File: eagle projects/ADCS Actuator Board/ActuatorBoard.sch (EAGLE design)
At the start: 231 parts, among them J11 TE_1-84953-1, J2 TE_1-84953-1, J4 TE_1-84953-1, J5 TE-1734829-3, U1 SIP2100DY-T1-GE3, U10 LM2917MX/NOPB, U12 TSV991AILT, U13 LM2917MX/NOPB, U14 ADS7841E_2K5, U16 DRV10970_MOTOR_DRIVERDRV10970, U17 LM2917MX/NOPB, U19 TSV991AILT, U2 SIP2100DY-T1-GE3, U20 ADS7841E_2K5, U3 SIP2100DY-T1-GE3, U6 DRV10970_MOTOR_DRIVERDRV10970, U7 DRV10970_MOTOR_DRIVERDRV10970, U8 TSV991AILT, U9 ADS7841E_2K5

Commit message: done
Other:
- note added: "ADCS Electrical"
- note added: "B"
- note added: "J. Smith, T.Christison"
- note added: "Maxon 351098"
- note removed: "A.1"
- note removed: "FIN 0 1 0 1 PWM 0 1 PWM"
- note removed: "OUT1 Hi-Z 1 0 0 1 !PWM !PWM 0"
- note removed: "OUT2 Hi-Z 0 1 0 !PWM 1 0 !PWM"
- note removed: "Operation Mode Stand-by Forward Reverse Brake Forward (PWM mode A) Reverse (PWM mode A) Forward (PWM mode B) Reverse (PWM mode B)"
- note removed: "RIN 0 0 1 1 0 PWM PWM 1"
- note removed: "VREF X VCC VCC X VCC VCC VCC VCC"

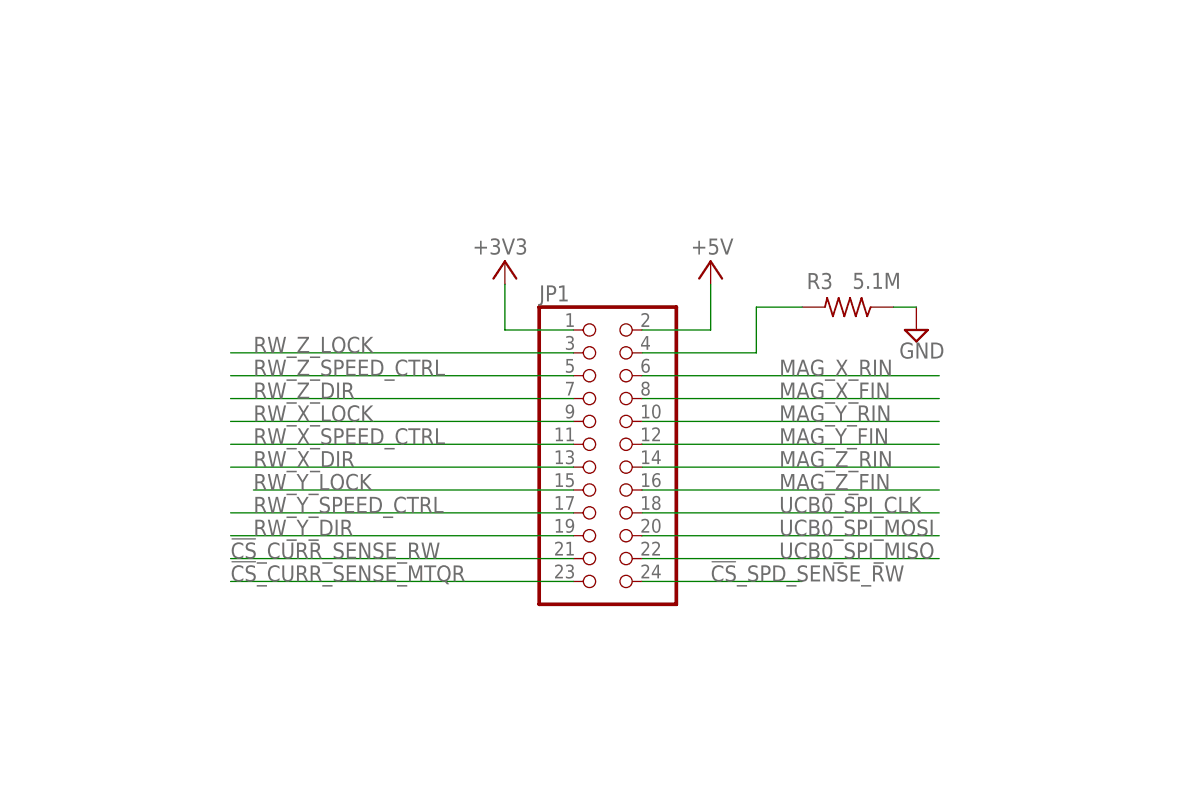
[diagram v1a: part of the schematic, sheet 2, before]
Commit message: Partially Replaced Connectors on Actuator
Will finish soon
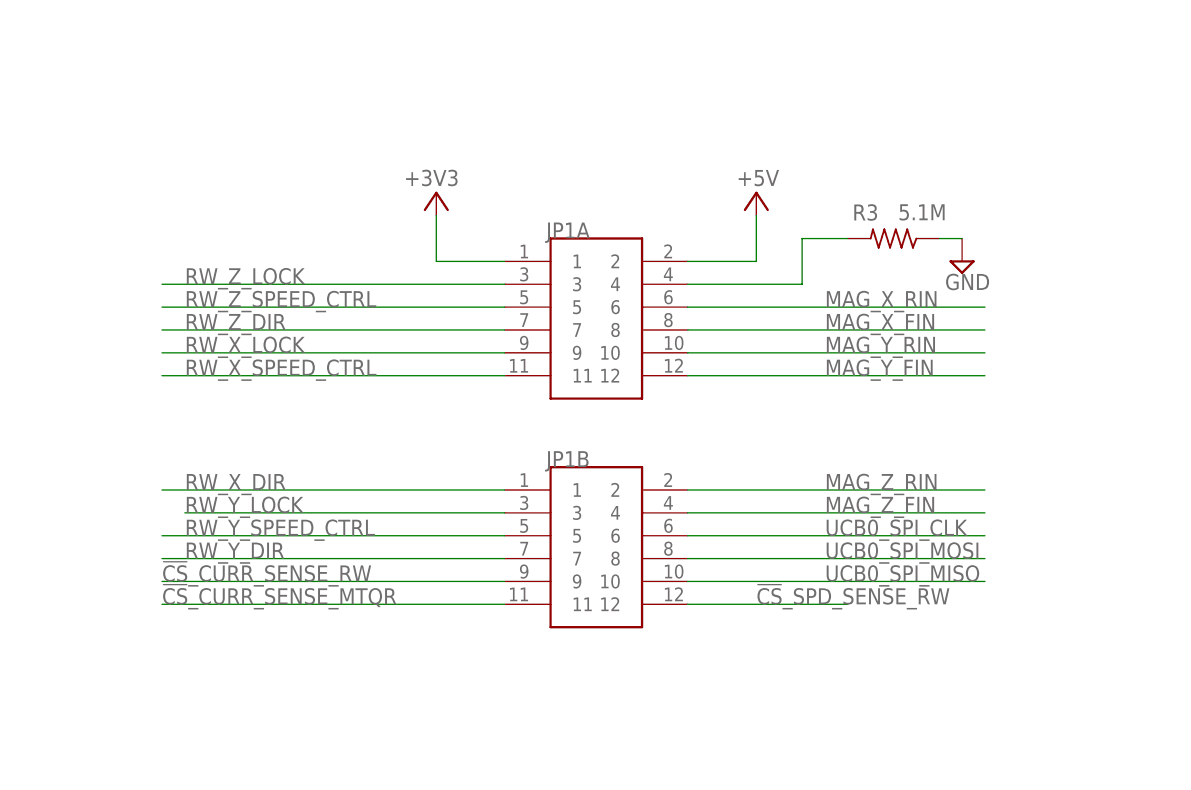
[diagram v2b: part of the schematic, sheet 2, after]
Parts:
- removed JP1: (no value), pinhead:PINHD-2X12
- added JP1A, JP1B: 832-10-012-10-005000, 832-10-012-10-005000:832-10-012-10-005000
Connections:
- net !CS!_CURR_SENSE_MTQR: now also JP1B.11; no longer JP1.23
- net !CS!_CURR_SENSE_RW: now also JP1B.9; no longer JP1.21
- net !CS!_SPD_SENSE_RW: now also JP1B.12; no longer JP1.24
- net +3V3: now also JP1A.1; no longer JP1.1
- net +5V: now also JP1A.2; no longer JP1.2
- net MAG_X_FIN: now also JP1A.8; no longer JP1.8
- net MAG_X_RIN: now also JP1A.6; no longer JP1.6
- net MAG_Y_FIN: now also JP1A.12; no longer JP1.12
- net MAG_Y_RIN: now also JP1A.10; no longer JP1.10
- net MAG_Z_FIN: now also JP1B.4; no longer JP1.16
- net MAG_Z_RIN: now also JP1B.2; no longer JP1.14
- net N$1: now also JP1A.4; no longer JP1.4
- net RW_X_DIR: now also JP1B.1; no longer JP1.13
- net RW_X_LOCK: now also JP1A.9; no longer JP1.9
- net RW_X_SPEED_CTRL: now also JP1A.11; no longer JP1.11
- net RW_Y_DIR: now also JP1B.7; no longer JP1.19
- net RW_Y_LOCK: now also JP1B.3; no longer JP1.15
- net RW_Y_SPEED_CTRL: now also JP1B.5; no longer JP1.17
- net RW_Z_DIR: now also JP1A.7; no longer JP1.7
- net RW_Z_LOCK: now also JP1A.3; no longer JP1.3
- net RW_Z_SPEED_CTRL: now also JP1A.5; no longer JP1.5
- net UCB0_SPI_CLK: now also JP1B.6; no longer JP1.18
- net UCB0_SPI_MISO: now also JP1B.10; no longer JP1.22
- net UCB0_SPI_MOSI: now also JP1B.8; no longer JP1.20
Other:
- moved on the sheet: R3

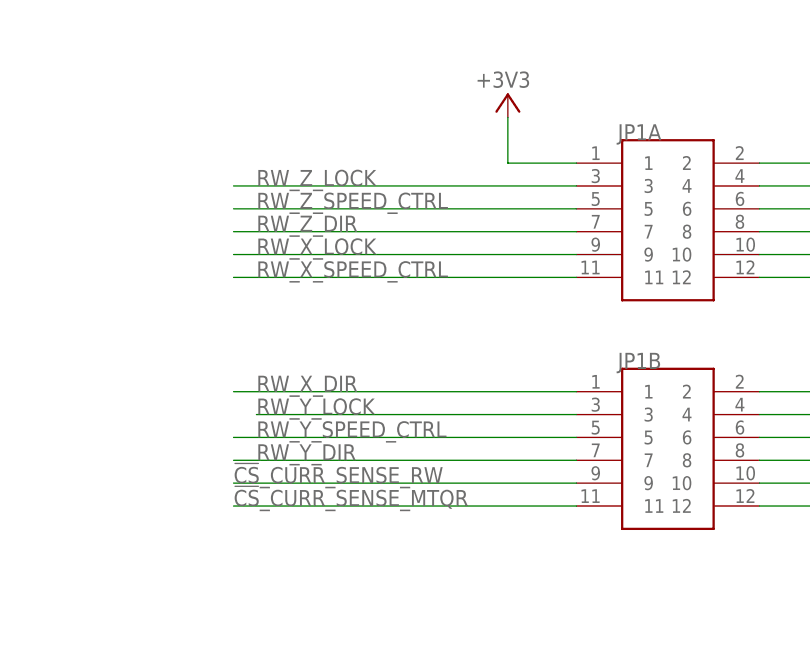
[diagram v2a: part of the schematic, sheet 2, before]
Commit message: Arranged 12x2 Connectors on Motherboard and Actuator Board
Unfinished, needs cleanup
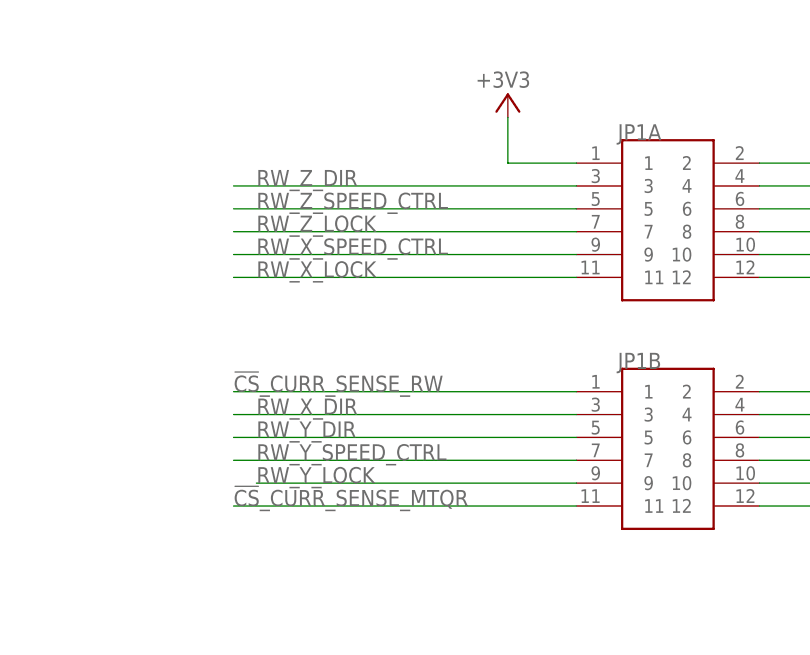
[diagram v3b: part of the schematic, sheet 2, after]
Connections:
- net !CS!_CURR_SENSE_RW: now also JP1B.1; no longer JP1B.9
- net RW_X_DIR: now also JP1B.3; no longer JP1B.1
- net RW_X_LOCK: now also JP1A.11; no longer JP1A.9
- net RW_X_SPEED_CTRL: now also JP1A.9; no longer JP1A.11
- net RW_Y_DIR: now also JP1B.5; no longer JP1B.7
- net RW_Y_LOCK: now also JP1B.9; no longer JP1B.3
- net RW_Y_SPEED_CTRL: now also JP1B.7; no longer JP1B.5
- net RW_Z_DIR: now also JP1A.3; no longer JP1A.7
- net RW_Z_LOCK: now also JP1A.7; no longer JP1A.3
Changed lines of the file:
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@@
 <net name="RW_X_DIR" class="0">
 <segment>
-<label x="119.38" y="129.54" size="1.778" layer="95"/>
-<wire x1="154.94" y1="129.54" x2="116.84" y2="129.54" width="0.1524" layer="91"/>
-<pinref part="JP1B" gate="G$1" pin="1"/>
+<label x="119.38" y="127" size="1.778" layer="95"/>
+<wire x1="154.94" y1="127" x2="116.84" y2="127" width="0.1524" layer="91"/>
+<pinref part="JP1B" gate="G$1" pin="3"/>
 </segment>
 </net>
 <net name="RW_X_SPEED_CTRL" class="0">
 <segment>
-<wire x1="154.94" y1="142.24" x2="116.84" y2="142.24" width="0.1524" layer="91"/>
-<label x="119.38" y="142.24" size="1.778" layer="95"/>
-<pinref part="JP1A" gate="G$1" pin="11"/>
+<wire x1="154.94" y1="144.78" x2="116.84" y2="144.78" width="0.1524" layer="91"/>
+<label x="119.38" y="144.78" size="1.778" layer="95"/>
+<pinref part="JP1A" gate="G$1" pin="9"/>
 </segment>
 </net>
 <net name="RW_Z_DIR" class="0">
 <segment>
-<wire x1="154.94" y1="147.32" x2="116.84" y2="147.32" width="0.1524" layer="91"/>
-<label x="119.38" y="147.32" size="1.778" layer="95"/>
-<pinref part="JP1A" gate="G$1" pin="7"/>
+<wire x1="154.94" y1="152.4" x2="116.84" y2="152.4" width="0.1524" layer="91"/>
+<label x="119.38" y="152.4" size="1.778" layer="95"/>
+<pinref part="JP1A" gate="G$1" pin="3"/>
 </segment>
 </net>
@@
 <net name="RW_Y_DIR" class="0">
 <segment>
+<wire x1="154.94" y1="124.46" x2="116.84" y2="124.46" width="0.1524" layer="91"/>
+<label x="119.38" y="124.46" size="1.778" layer="95"/>
+<pinref part="JP1B" gate="G$1" pin="5"/>
+</segment>
+</net>
+<net name="RW_Y_SPEED_CTRL" class="0">
+<segment>
+<label x="119.38" y="121.92" size="1.778" layer="95"/>
 <wire x1="154.94" y1="121.92" x2="116.84" y2="121.92" width="0.1524" layer="91"/>
-<label x="119.38" y="121.92" size="1.778" layer="95"/>
 <pinref part="JP1B" gate="G$1" pin="7"/>
-</segment>
-</net>
-<net name="RW_Y_SPEED_CTRL" class="0">
-<segment>
-<label x="119.38" y="124.46" size="1.778" layer="95"/>
-<wire x1="154.94" y1="124.46" x2="116.84" y2="124.46" width="0.1524" layer="91"/>
-<pinref part="JP1B" gate="G$1" pin="5"/>
 </segment>
 </net>
@@
 <net name="RW_Y_LOCK" class="0">
 <segment>
-<wire x1="119.38" y1="127" x2="154.94" y2="127" width="0.1524" layer="91"/>
-<label x="119.38" y="127" size="1.778" layer="95"/>
-<pinref part="JP1B" gate="G$1" pin="3"/>
+<wire x1="119.38" y1="119.38" x2="154.94" y2="119.38" width="0.1524" layer="91"/>
+<label x="119.38" y="119.38" size="1.778" layer="95"/>
+<pinref part="JP1B" gate="G$1" pin="9"/>
 </segment>
 </net>
 <net name="!CS!_CURR_SENSE_RW" class="0">
 <segment>
-<label x="116.84" y="119.38" size="1.778" layer="95"/>
-<wire x1="154.94" y1="119.38" x2="116.84" y2="119.38" width="0.1524" layer="91"/>
-<pinref part="JP1B" gate="G$1" pin="9"/>
+<label x="116.84" y="129.54" size="1.778" layer="95"/>
+<wire x1="154.94" y1="129.54" x2="116.84" y2="129.54" width="0.1524" layer="91"/>
+<pinref part="JP1B" gate="G$1" pin="1"/>
 </segment>
 </net>
@@
 <net name="RW_X_LOCK" class="0">
 <segment>
-<wire x1="116.84" y1="144.78" x2="154.94" y2="144.78" width="0.1524" layer="91"/>
-<label x="119.38" y="144.78" size="1.778" layer="95"/>
-<pinref part="JP1A" gate="G$1" pin="9"/>
+<wire x1="116.84" y1="142.24" x2="154.94" y2="142.24" width="0.1524" layer="91"/>
+<label x="119.38" y="142.24" size="1.778" layer="95"/>
+<pinref part="JP1A" gate="G$1" pin="11"/>
 </segment>
 </net>
@@
 <net name="RW_Z_LOCK" class="0">
 <segment>
-<wire x1="154.94" y1="152.4" x2="116.84" y2="152.4" width="0.1524" layer="91"/>
-<label x="119.38" y="152.4" size="1.778" layer="95"/>
-<pinref part="JP1A" gate="G$1" pin="3"/>
-</segment>
-</net>
+<wire x1="154.94" y1="147.32" x2="116.84" y2="147.32" width="0.1524" layer="91"/>
+<label x="119.38" y="147.32" size="1.778" layer="95"/>
+<pinref part="JP1A" gate="G$1" pin="7"/>
+</segment>
+</net>

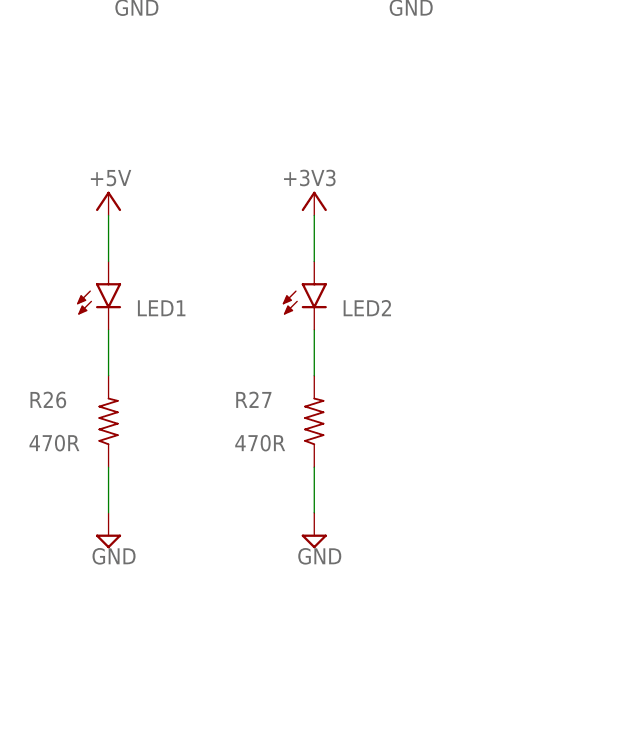
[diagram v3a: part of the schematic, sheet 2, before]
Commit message: Removed LEDs from actuator board
Removed power reader LEDs from actuator boards.  Associated resistors were also removed and BOM was updated.
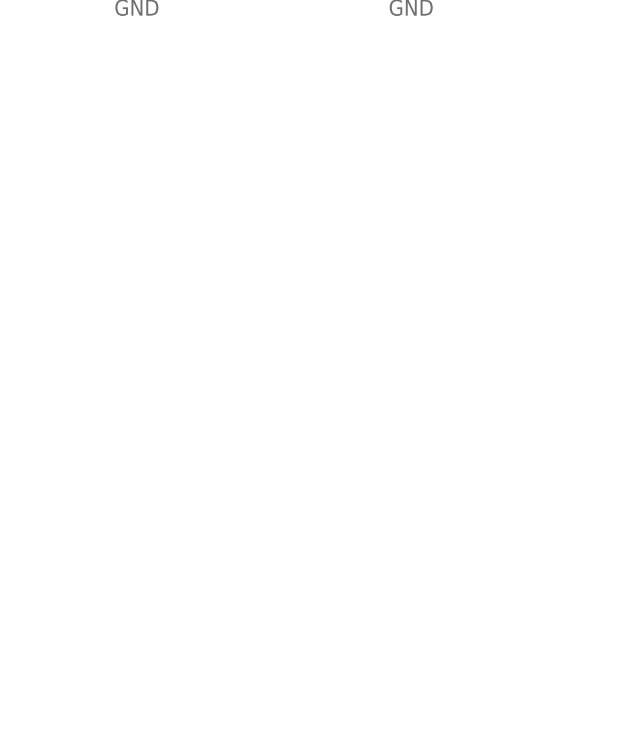
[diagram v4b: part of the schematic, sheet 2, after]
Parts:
- removed LED1, LED2: (no value), led:LEDCHIPLED_0603
- removed R26, R27: 470R, rcl:R-US_R0603
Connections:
- removed net N$14: LED2.C, R27.2
- removed net N$5: LED1.C, R26.2
- net +3V3: no longer LED2.A
- net +5V: no longer LED1.A
- net GND: no longer R26.1, R27.1
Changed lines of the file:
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@@
 <groups>
 <schematic_group name="POWER"/>
-<schematic_group name="INDICATOR_LEDS_POWER"/>
 <schematic_group name="BOARD_MOUNTING_HOLES"/>
 <schematic_group name="TIA_BIASING1"/>
@@
 <part name="P+47" library="supply1" library_urn="urn:adsk.eagle:library:371" deviceset="+5V" device=""/>
 <part name="SUPPLY37" library="supply2" library_urn="urn:adsk.eagle:library:372" deviceset="GND" device=""/>
-<part name="SUPPLY41" library="supply2" library_urn="urn:adsk.eagle:library:372" deviceset="GND" device=""/>
-<part name="R26" library="rcl" library_urn="urn:adsk.eagle:library:334" deviceset="R-US_" device="R0603" package3d_urn="urn:adsk.eagle:package:23555/3" value="470R"/>
-<part name="SUPPLY44" library="supply2" library_urn="urn:adsk.eagle:library:372" deviceset="GND" device=""/>
-<part name="R27" library="rcl" library_urn="urn:adsk.eagle:library:334" deviceset="R-US_" device="R0603" package3d_urn="urn:adsk.eagle:package:23555/3" value="470R"/>
-<part name="LED1" library="led" library_urn="urn:adsk.eagle:library:259" deviceset="LED" device="CHIPLED_0603" package3d_urn="urn:adsk.eagle:package:15822/2"/>
-<part name="LED2" library="led" library_urn="urn:adsk.eagle:library:259" deviceset="LED" device="CHIPLED_0603" package3d_urn="urn:adsk.eagle:package:15822/2"/>
-<part name="P+30" library="supply1" library_urn="urn:adsk.eagle:library:371" deviceset="+5V" device=""/>
-<part name="+3V27" library="supply1" library_urn="urn:adsk.eagle:library:371" deviceset="+3V3" device=""/>
 <part name="RWZ" library="my_library" library_urn="urn:adsk.eagle:library:22876504" deviceset="REACTION_WHEEL_NOPINS_MAXON" device="" package3d_urn="urn:adsk.eagle:package:26139267/6"/>
 <part name="MX" library="my_library" library_urn="urn:adsk.eagle:library:22876504" deviceset="NCTR-M002_MAGNETORQUER" device="" package3d_urn="urn:adsk.eagle:package:26139365/2"/>
@@
 <attribute name="REVIEWER" x="196.85" y="6.35" size="2.54" layer="94"/>
 </instance>
-<instance part="SUPPLY41" gate="GND" x="30.48" y="119.38" smashed="yes" grouprefs="INDICATOR_LEDS_POWER">
-<attribute name="VALUE" x="28.575" y="116.205" size="1.778" layer="96"/>
-</instance>
-<instance part="R26" gate="G$1" x="30.48" y="132.08" smashed="yes" rot="R90" grouprefs="INDICATOR_LEDS_POWER">
-<attribute name="NAME" x="21.59" y="133.5786" size="1.778" layer="95"/>
-<attribute name="VALUE" x="21.59" y="128.778" size="1.778" layer="96"/>
-</instance>
-<instance part="SUPPLY44" gate="GND" x="53.34" y="119.38" smashed="yes" grouprefs="INDICATOR_LEDS_POWER">
-<attribute name="VALUE" x="51.435" y="116.205" size="1.778" layer="96"/>
-</instance>
-<instance part="R27" gate="G$1" x="53.34" y="132.08" smashed="yes" rot="R90" grouprefs="INDICATOR_LEDS_POWER">
-<attribute name="NAME" x="44.45" y="133.5786" size="1.778" layer="95"/>
-<attribute name="VALUE" x="44.45" y="128.778" size="1.778" layer="96"/>
-</instance>
-<instance part="LED1" gate="G$1" x="30.48" y="147.32" smashed="yes" grouprefs="INDICATOR_LEDS_POWER">
-<attribute name="NAME" x="33.528" y="143.764" size="1.778" layer="95"/>
-<attribute name="VALUE" x="36.195" y="142.748" size="1.778" layer="96" rot="R90"/>
-</instance>
-<instance part="LED2" gate="G$1" x="53.34" y="147.32" smashed="yes" grouprefs="INDICATOR_LEDS_POWER">
-<attribute name="NAME" x="56.388" y="143.764" size="1.778" layer="95"/>
-<attribute name="VALUE" x="59.055" y="142.748" size="1.778" layer="96" rot="R90"/>
-</instance>
-<instance part="P+30" gate="1" x="30.48" y="157.48" smashed="yes" grouprefs="INDICATOR_LEDS_POWER">
-<attribute name="VALUE" x="33.02" y="160.02" size="1.778" layer="96" rot="R180"/>
-</instance>
-<instance part="+3V27" gate="G$1" x="53.34" y="157.48" smashed="yes" grouprefs="INDICATOR_LEDS_POWER">
-<attribute name="VALUE" x="55.88" y="160.02" size="1.778" layer="96" rot="R180"/>
-</instance>
 <instance part="P+13" gate="1" x="182.88" y="162.56" smashed="yes">
 <attribute name="VALUE" x="185.42" y="165.1" size="1.778" layer="96" rot="R180"/>
@@
 </segment>
 <segment>
-<pinref part="SUPPLY41" gate="GND" pin="GND"/>
-<pinref part="R26" gate="G$1" pin="1"/>
-<wire x1="30.48" y1="121.92" x2="30.48" y2="127" width="0.1524" layer="91" grouprefs="INDICATOR_LEDS_POWER"/>
-</segment>
-<segment>
-<pinref part="SUPPLY44" gate="GND" pin="GND"/>
-<pinref part="R27" gate="G$1" pin="1"/>
-<wire x1="53.34" y1="121.92" x2="53.34" y2="127" width="0.1524" layer="91" grouprefs="INDICATOR_LEDS_POWER"/>
-</segment>
-<segment>
 <pinref part="SUPPLY94" gate="GND" pin="GND"/>
 <pinref part="U9" gate="A" pin="COM"/>
@@
 </segment>
 <segment>
-<pinref part="LED1" gate="G$1" pin="A"/>
-<pinref part="P+30" gate="1" pin="+5V"/>
-<wire x1="30.48" y1="149.86" x2="30.48" y2="154.94" width="0.1524" layer="91" grouprefs="INDICATOR_LEDS_POWER"/>
-</segment>
-<segment>
 <wire x1="175.26" y1="154.94" x2="182.88" y2="154.94" width="0.1524" layer="91"/>
 <pinref part="P+13" gate="1" pin="+5V"/>
@@
 </segment>
 <segment>
-<pinref part="LED2" gate="G$1" pin="A"/>
-<pinref part="+3V27" gate="G$1" pin="+3V3"/>
-<wire x1="53.34" y1="149.86" x2="53.34" y2="154.94" width="0.1524" layer="91" grouprefs="INDICATOR_LEDS_POWER"/>
-</segment>
-<segment>
 <pinref part="R5" gate="G$1" pin="2"/>
 <wire x1="139.7" y1="50.8" x2="157.48" y2="50.8" width="0.1524" layer="91"/>
@@
 </segment>
 </net>
-<net name="N$5" class="0">
-<segment>
-<pinref part="R26" gate="G$1" pin="2"/>
-<pinref part="LED1" gate="G$1" pin="C"/>
-<wire x1="30.48" y1="137.16" x2="30.48" y2="142.24" width="0.1524" layer="91" grouprefs="INDICATOR_LEDS_POWER"/>
-</segment>
-</net>
-<net name="N$14" class="0">
-<segment>
-<pinref part="R27" gate="G$1" pin="2"/>
-<pinref part="LED2" gate="G$1" pin="C"/>
-<wire x1="53.34" y1="137.16" x2="53.34" y2="142.24" width="0.1524" layer="91" grouprefs="INDICATOR_LEDS_POWER"/>
-</segment>
-</net>
